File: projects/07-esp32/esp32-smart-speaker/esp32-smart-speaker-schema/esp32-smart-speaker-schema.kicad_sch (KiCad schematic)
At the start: 14 parts, among them SW1 SW_Push_Dual, SW2 SW_Push_Dual, SW3 SW_Push_Dual, SW4 SW_Push_Dual, SW5 SW_Push_Dual, U2 MAX98357A

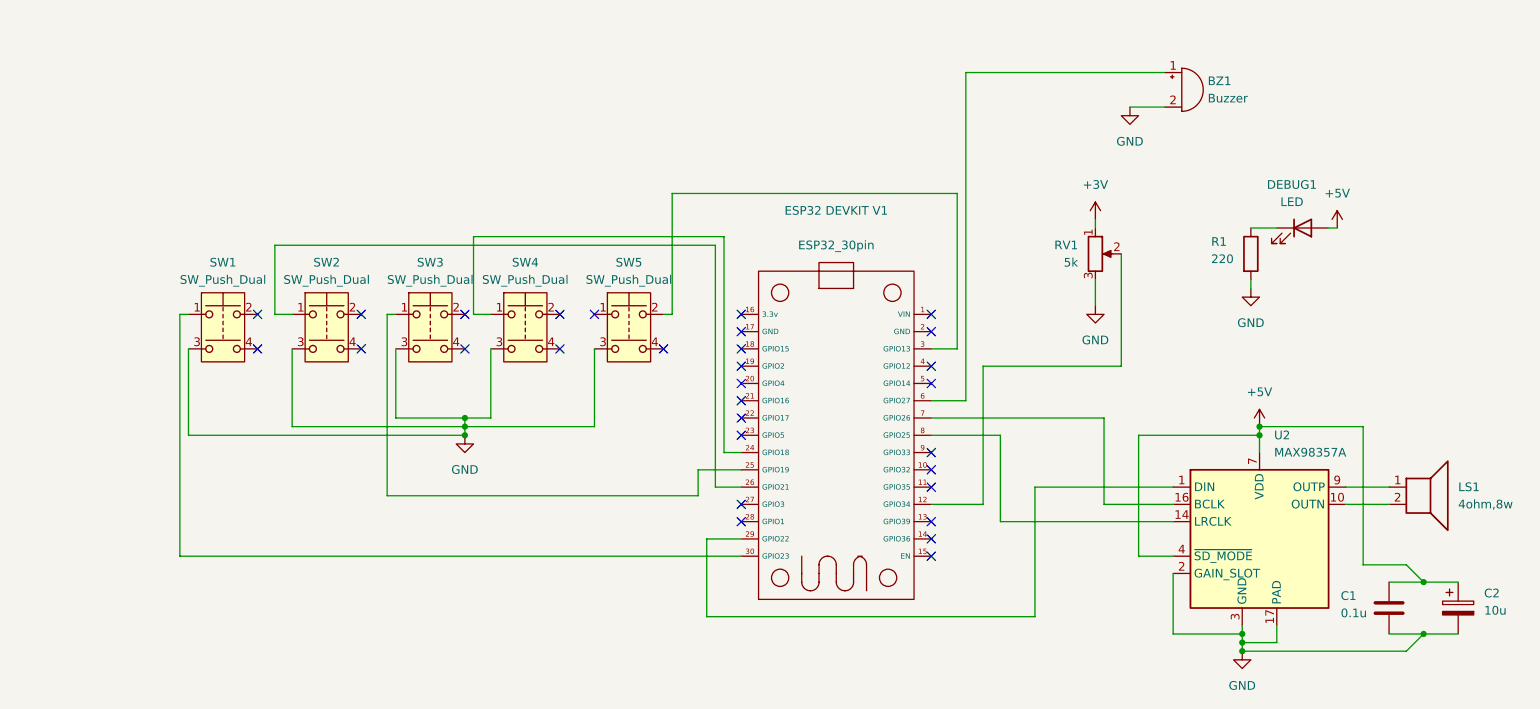
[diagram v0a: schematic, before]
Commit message: Added more features to esp32-smart-speaker project
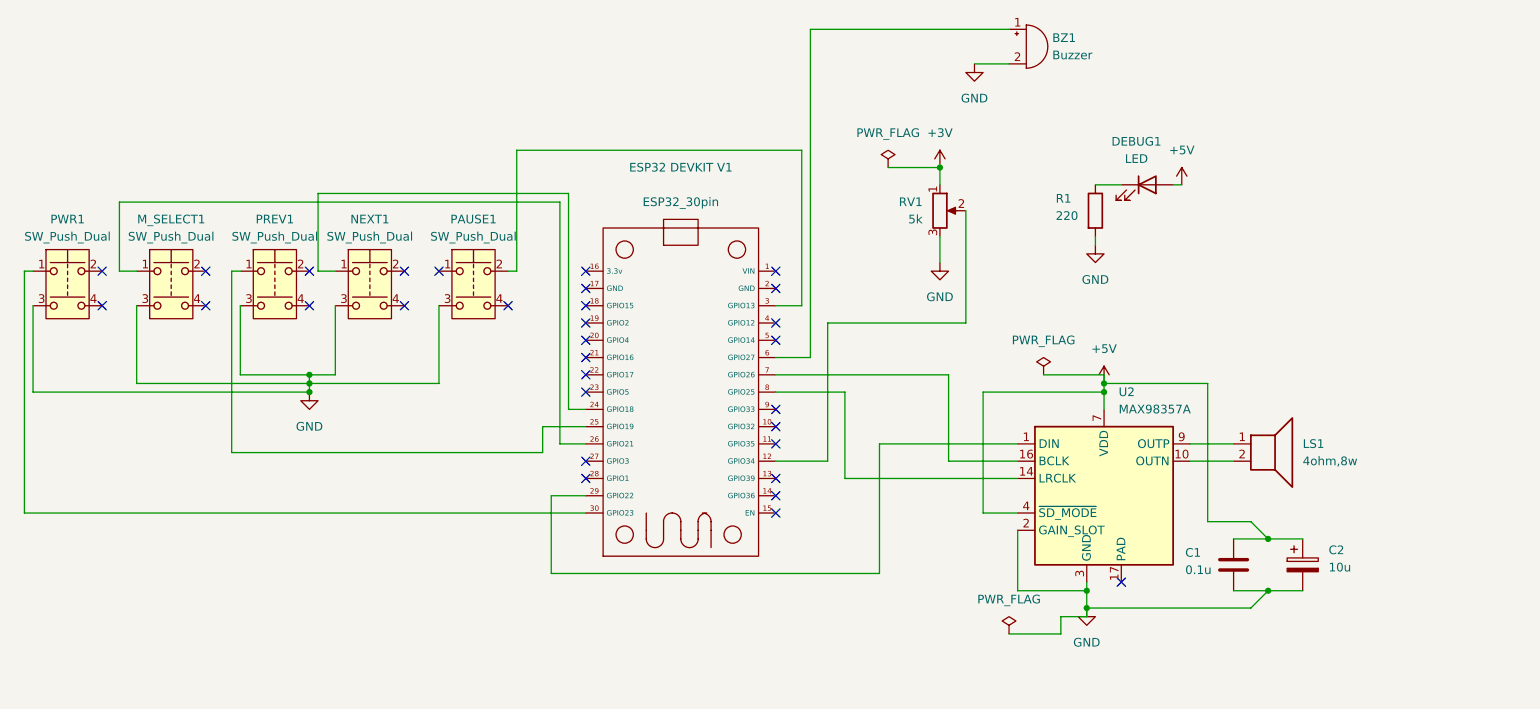
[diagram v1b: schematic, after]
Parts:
- renumbered SW2 to M_SELECT1, SW4 to NEXT1, SW5 to PAUSE1, SW3 to PREV1, SW1 to PWR1
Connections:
- net GND: no longer U2.17 (PAD)
- no-connect marks 30 -> 31
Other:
- moved on the sheet: BZ1, C1, C2, DEBUG1, ESP32 DEVKIT V1, LS1, M_SELECT1, NEXT1, PAUSE1, PREV1, PWR1, R1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
